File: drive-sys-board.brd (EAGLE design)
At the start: 109.2 x 49.5 mm, 31 parts, among them J2 APP_2POS_CONFIG12V_HORIZ, U1 OKI-78SR-5/1.5-W36HC, U2 MAX232, U3 MAX232, U4 MAX232

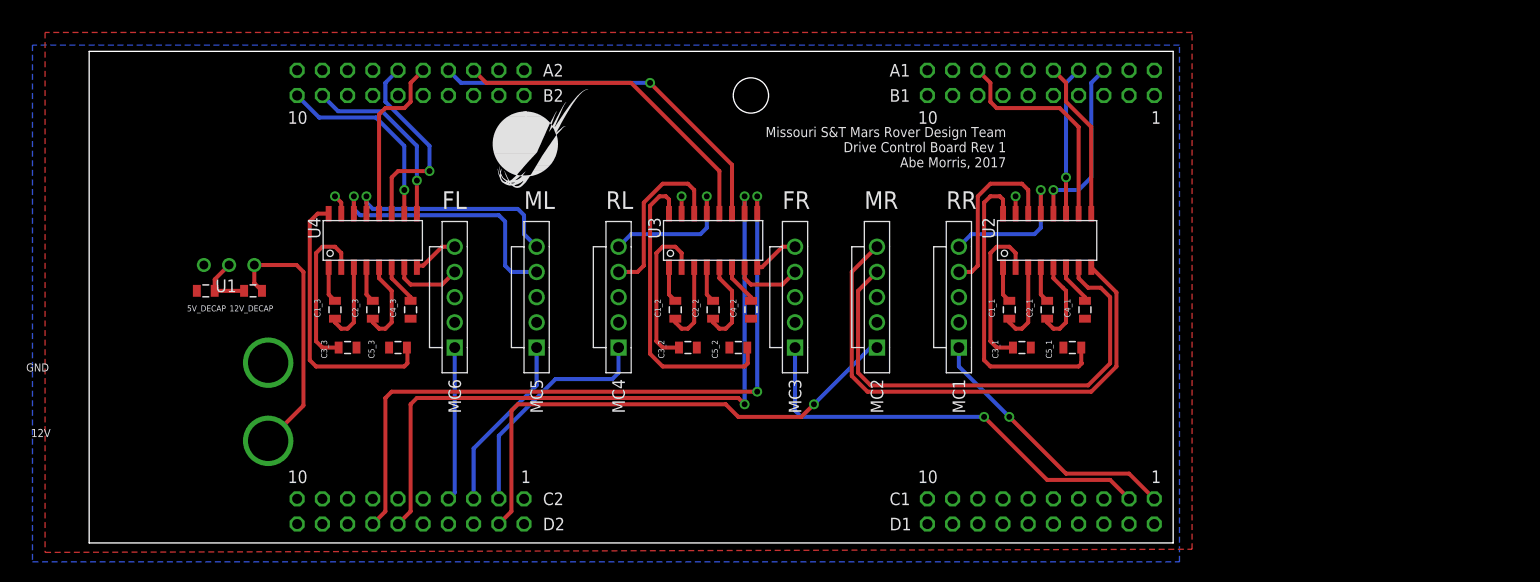
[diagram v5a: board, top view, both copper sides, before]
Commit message: Moved silkscreen labels
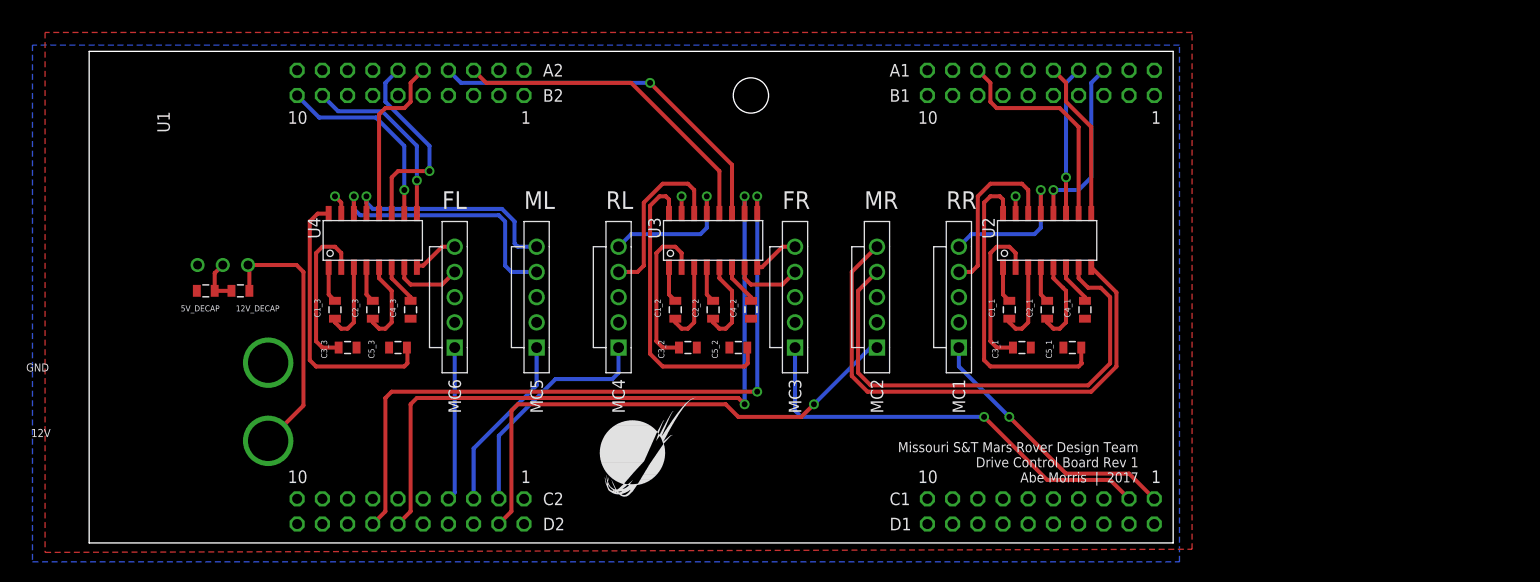
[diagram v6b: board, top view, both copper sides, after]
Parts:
- moved U$2 32.9 mm to (52.1, 3.17)
- moved 12V_DECAP 1.27 mm to (15.9, 24.8)
- moved U1 0.63 mm to (16.6, 27.4)
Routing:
- net GND: track 11.7 -> 10.1 mm
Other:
- board text added: "Missouri S&T Mars Rover Design Team Drive Control Board Rev 1 Abe Morris | 2017"
- board text removed: "Missouri S&T Mars Rover Design Team Drive Control Board Rev 1 Abe Morris, 2017"
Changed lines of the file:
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@@
 <wire x1="109.855" y1="48.895" x2="0.635" y2="48.895" width="0" layer="20"/>
 <wire x1="0.635" y1="48.895" x2="0.635" y2="-0.635" width="0" layer="20"/>
-<text x="93.0275" y="41.275" size="1.016" layer="21" font="vector" rot="R180">Missouri S&amp;T Mars Rover Design Team
+<text x="106.3625" y="9.525" size="1.016" layer="21" font="vector" rot="R180">Missouri S&amp;T Mars Rover Design Team
 Drive Control Board Rev 1
-Abe Morris, 2017                                </text>
+Abe Morris  |  2017                                </text>
 <dimension x1="0" y1="0" x2="109.22" y2="0" x3="54.61" y3="-12.065" textsize="1.778" layer="47" dtype="horizontal" unit="inch" precision="6" visible="yes"/>
 <dimension x1="109.22" y1="0" x2="109.22" y2="48.26" x3="124.46" y3="24.13" textsize="1.778" layer="47" dtype="horizontal" unit="inch" precision="6" visible="yes"/>
@@
 <elements>
 <element name="U$1" library="MRDT-2015-General" package="TIVA-C-CONNECTED" value="TIVA-C-CONNECTED" x="-15.24" y="-7.62" smashed="yes"/>
-<element name="U$2" library="MRDT-2015-General" package="MRDT_LOGO" value="" x="41.275" y="34.29"/>
-<element name="U1" library="MRDT-ICs" package="OKI-78SR_HORIZ" value="OKI-78SR-5/1.5-W36HC" x="17.272" y="27.3685" smashed="yes">
-<attribute name="VOUT" value="+5v" x="17.272" y="27.3685" size="1.778" layer="27" display="off"/>
-<attribute name="NAME" x="15.494" y="25.908" size="1.27" layer="25" font="vector" rot="R180"/>
+<element name="U$2" library="MRDT-2015-General" package="MRDT_LOGO" value="" x="52.07" y="3.175"/>
+<element name="U1" library="MRDT-ICs" package="OKI-78SR_HORIZ" value="OKI-78SR-5/1.5-W36HC" x="16.637" y="27.3685" smashed="yes">
+<attribute name="VOUT" value="+5v" x="16.637" y="27.3685" size="1.778" layer="27" display="off"/>
+<attribute name="NAME" x="8.763" y="40.7035" size="1.27" layer="25" font="vector" rot="R90"/>
 </element>
 <element name="J2" library="MRDT-Connectors" package="APP45_12V_HORIZ_CONFIG" value="APP_2POS_CONFIG12V_HORIZ" x="-9.525" y="5.715">
@@
 </element>
 <element name="5V_DECAP" library="SparkFun-Capacitors" package="0805" value="10uF" x="12.3825" y="24.765" smashed="yes" rot="R180">
-<attribute name="NAME" x="14.4145" y="23.3045" size="0.6096" layer="25" font="vector" rot="R180"/>
+<attribute name="NAME" x="13.7795" y="23.3045" size="0.6096" layer="25" font="vector" rot="R180"/>
 <attribute name="VALUE" x="13.3985" y="26.162" size="0.4064" layer="27" rot="R180"/>
 </element>
-<element name="12V_DECAP" library="SparkFun-Capacitors" package="0805" value="10uF" x="17.145" y="24.765" smashed="yes" rot="R180">
-<attribute name="NAME" x="19.177" y="23.3045" size="0.6096" layer="25" font="vector" rot="R180"/>
-<attribute name="VALUE" x="18.161" y="26.162" size="0.4064" layer="27" rot="R180"/>
+<element name="12V_DECAP" library="SparkFun-Capacitors" package="0805" value="10uF" x="15.875" y="24.765" smashed="yes" rot="R180">
+<attribute name="NAME" x="19.812" y="23.3045" size="0.6096" layer="25" font="vector" rot="R180"/>
+<attribute name="VALUE" x="16.891" y="26.162" size="0.4064" layer="27" rot="R180"/>
 </element>
 </elements>
@@
 <wire x1="93.98" y1="32.545" x2="93.98" y2="34.29" width="0.4064" layer="1"/>
 <via x="93.98" y="34.29" extent="1-16" drill="0.6" shape="square"/>
-<wire x1="16.245" y1="24.765" x2="13.2825" y2="24.765" width="0.4064" layer="1"/>
-<wire x1="14.732" y1="27.3685" x2="13.2825" y2="25.919" width="0.4064" layer="1"/>
-<wire x1="13.2825" y1="25.919" x2="13.2825" y2="24.765" width="0.4064" layer="1"/>
+<wire x1="14.975" y1="24.765" x2="13.2825" y2="24.765" width="0.4064" layer="1"/>
+<wire x1="14.097" y1="27.3685" x2="13.2825" y2="26.554" width="0.4064" layer="1"/>
+<wire x1="13.2825" y1="26.554" x2="13.2825" y2="24.765" width="0.4064" layer="1"/>
 </signal>
 <signal name="TX_1">
@@
 <wire x1="22.225" y1="13.208" x2="22.225" y2="26.67" width="0.4064" layer="1"/>
 <wire x1="22.225" y1="26.67" x2="21.5265" y2="27.3685" width="0.4064" layer="1"/>
-<wire x1="21.5265" y1="27.3685" x2="17.272" y2="27.3685" width="0.4064" layer="1"/>
-<wire x1="18.045" y1="24.765" x2="17.272" y2="25.538" width="0.4064" layer="1"/>
-<wire x1="17.272" y1="25.538" x2="17.272" y2="27.3685" width="0.4064" layer="1"/>
+<wire x1="21.5265" y1="27.3685" x2="16.637" y2="27.3685" width="0.4064" layer="1"/>
+<wire x1="16.775" y1="24.765" x2="16.775" y2="27.2305" width="0.4064" layer="1"/>
+<wire x1="16.775" y1="27.2305" x2="16.637" y2="27.3685" width="0.4064" layer="1"/>
 </signal>
 <signal name="N$3">
@@
 <wire x1="28.575" y1="34.29" x2="28.575" y2="33.655" width="0.4064" layer="16"/>
 <wire x1="28.575" y1="33.655" x2="29.21" y2="33.02" width="0.4064" layer="16"/>
-<wire x1="29.21" y1="33.02" x2="43.815" y2="33.02" width="0.4064" layer="16"/>
-<wire x1="43.815" y1="33.02" x2="44.45" y2="32.385" width="0.4064" layer="16"/>
-<wire x1="44.45" y1="32.385" x2="44.45" y2="30.48" width="0.4064" layer="16"/>
-<wire x1="44.45" y1="30.48" x2="45.72" y2="29.21" width="0.4064" layer="16"/>
+<wire x1="29.21" y1="33.02" x2="42.2275" y2="33.02" width="0.4064" layer="16"/>
+<wire x1="42.2275" y1="33.02" x2="43.4975" y2="31.75" width="0.4064" layer="16"/>
+<wire x1="43.4975" y1="31.75" x2="43.4975" y2="29.5275" width="0.4064" layer="16"/>
+<wire x1="43.4975" y1="29.5275" x2="43.815" y2="29.21" width="0.4064" layer="16"/>
+<wire x1="43.815" y1="29.21" x2="45.72" y2="29.21" width="0.4064" layer="16"/>
 </signal>
 <signal name="N$30">

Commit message: Made board slightly larger
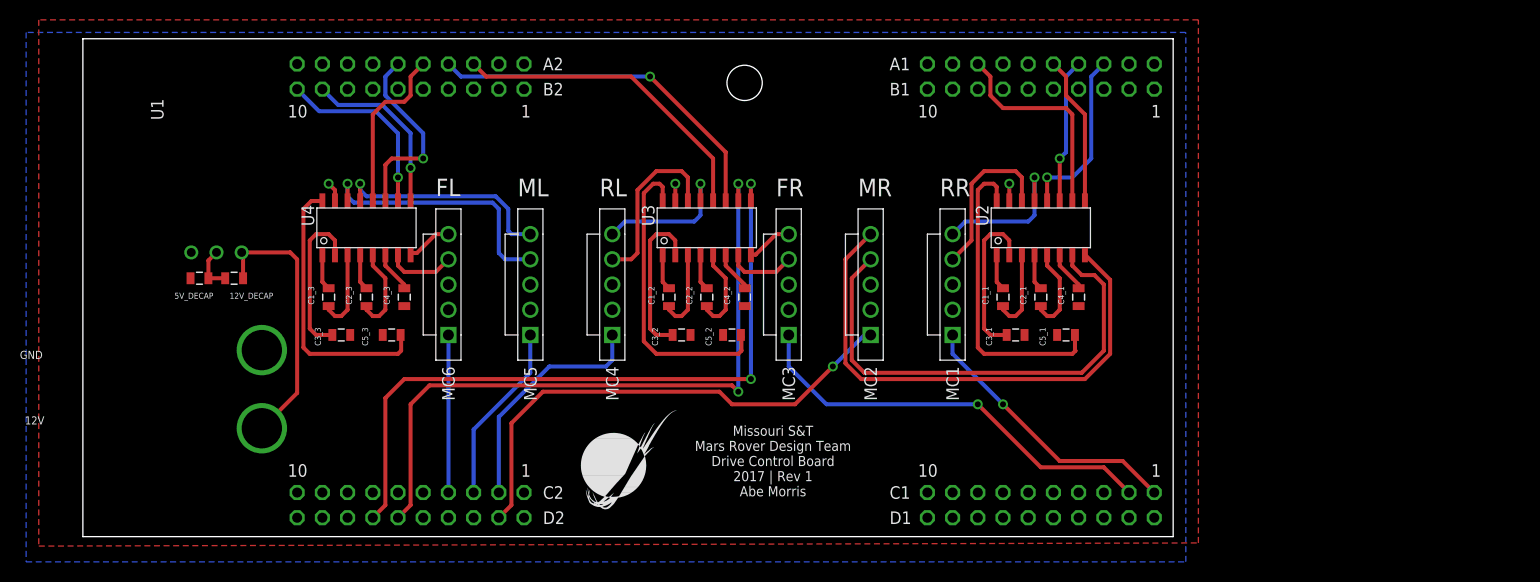
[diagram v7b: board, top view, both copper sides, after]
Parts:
- moved U$2 2.29 mm to (50.2, 1.91)
- moved C1_1 1.42 mm to (92.7, 24.1)
- moved C2_1 1.42 mm to (96.5, 24.1)
- moved C4_1 1.42 mm to (100.3, 24.1)
- moved C4_2 1.42 mm to (66.7, 24.1)
- moved C4_3 1.42 mm to (32.4, 24.1)
- moved C5_2 1.42 mm to (65.4, 20.3)
- moved MC1 1.42 mm to (87.6, 25.4)
- moved MC2 1.42 mm to (79.4, 25.4)
- moved MC6 1.42 mm to (36.8, 25.4)
- moved U2 1.42 mm to (96.5, 31.1)
- moved J2 1.42 mm to (-10.2, 6.99)
- moved C2_3 1.42 mm to (28.6, 24.1)
- moved C3_3 1.42 mm to (26.0, 20.3)
- moved C5_3 1.42 mm to (31.1, 20.3)
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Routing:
- net PWM_2: track 52.5 -> 51.0 mm
- net PWM_3: track 43.7 -> 42.7 mm
- net TX_3: track 37.4 -> 36.5 mm
- net PWM_1: track 27.1 -> 28.0 mm
- net TX_5: track 20.3 -> 19.4 mm
- net RX_3: track 33.3 -> 32.4 mm
- net TX_6: track 19.7 -> 18.8 mm
- net TX_2: track 22.4 -> 21.5 mm
- net RX_6: track 18.8 -> 17.9 mm
- net RX_2: track 16.0 -> 15.1 mm
- net TX_4: track 69.5 -> 68.7 mm
- net N$36: track 17.4 -> 16.7 mm
- net RX_4: track 72.4 -> 71.6 mm
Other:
- board size 109.2 x 49.5 mm -> 109.9 x 50.2 mm
- board text added: "Missouri S&T Mars Rover Design Team Drive Control Board 2017 | Rev 1 Abe Morris"
- board text removed: "Missouri S&T Mars Rover Design Team Drive Control Board Rev 1 Abe Morris | 2017"

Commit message: Changed serial pairs to match Tiva hardware
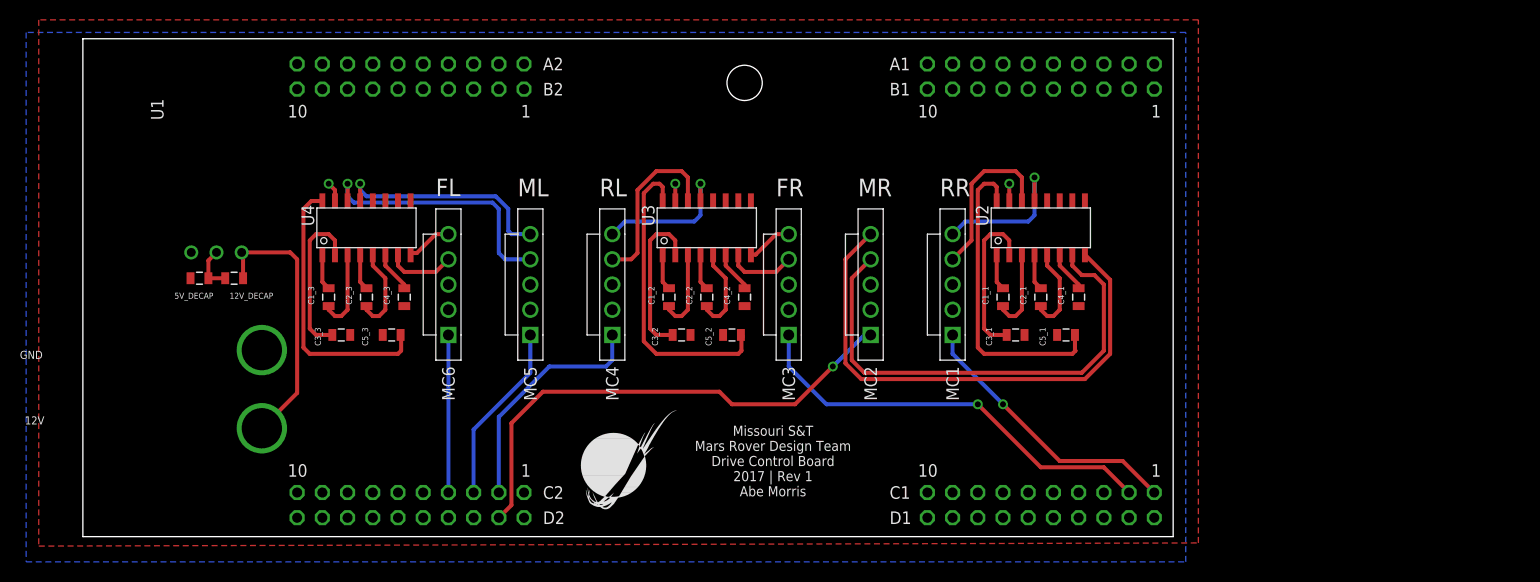
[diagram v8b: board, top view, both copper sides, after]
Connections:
- net RX_1: now also U$1.PA6; no longer U$1.PC4
- net RX_2: now also U$1.PA4; no longer U$1.PC6
- net RX_3: now also U$1.PK0; no longer U$1.PP0
- net RX_4: now also U$1.PC6; no longer U$1.PQ3/PA2
- net RX_5: now also U$1.PP0; no longer U$1.PD4
- net RX_6: now also U$1.PC4; no longer U$1.PA4
- net TX_1: now also U$1.PA7; no longer U$1.PC5
- net TX_2: now also U$1.PA5; no longer U$1.PC7
- net TX_3: now also U$1.PK1; no longer U$1.PP1
- net TX_4: now also U$1.PC7; no longer U$1.PQ2/PA3
- net TX_5: now also U$1.PP1; no longer U$1.PD5
- net TX_6: now also U$1.PC5; no longer U$1.PA5
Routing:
- net RX_4: track 71.6 -> 0.00 mm, vias 2 -> 0
- net TX_4: track 68.7 -> 0.00 mm, vias 2 -> 0
- net TX_3: track 36.5 -> 0.00 mm, vias 1 -> 0
- net RX_3: track 32.4 -> 0.00 mm
- net TX_2: track 21.5 -> 0.00 mm
- net TX_5: track 19.4 -> 0.00 mm, vias 1 -> 0
- net TX_6: track 18.8 -> 0.00 mm, vias 1 -> 0
- net RX_6: track 17.9 -> 0.00 mm, vias 1 -> 0
- net RX_1: track 17.7 -> 0.00 mm, vias 1 -> 0
- net RX_5: track 17.0 -> 0.00 mm
- net RX_2: track 15.1 -> 0.00 mm
- net TX_1: track 14.6 -> 0.00 mm, vias 1 -> 0
